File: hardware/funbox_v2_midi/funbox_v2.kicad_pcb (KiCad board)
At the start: 2 copper layers, 59.7 x 67.5 mm, 70 parts, among them J6 MIDI IN, J7 MIDI OUT, SW1 SW_SPDT, SW2 SW_SPDT, SW3 SW_SPDT, U1 TL074, U2 L7805, U5 H11L1

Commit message: Updated version2 pcb. Updated expression for Jupiter, Neptune, and Pluto
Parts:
- moved J7 1.85 mm to (175.8, 71.2)
- moved DipSwitch 1.82 mm to (124.1, 117.0)
- moved J6 1.62 mm to (119.9, 71.2)
- moved R31 0.96 mm to (154.4, 72.8)
- moved R33 0.96 mm to (162.1, 69.7)
- moved C6 0.45 mm to (131.1, 122.1)
- moved R32 0.28 mm to (141.4, 70.1)
- moved D2 0.27 mm to (133.8, 73.0)
- moved R30 0.27 mm to (133.8, 67.1)
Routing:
- net FOOT_SWITCH_2: track 77.6 -> 72.4 mm
- net DIP2: track 30.1 -> 25.5 mm
- net DIP1: track 23.9 -> 25.7 mm
- net MIDI_OUT_JACK_PIN5: track 27.4 -> 25.7 mm
- net MIDI_OUT: track 19.5 -> 21.1 mm
- net MIDI_IN_JACK_PIN5: track 17.7 -> 16.2 mm
- net DIP3: track 39.9 -> 38.6 mm
- net DIP4: track 41.0 -> 39.7 mm
- net MIDI_IN_JACK_PIN4: track 10.9 -> 9.74 mm
- net MIDI_IN: track 38.0 -> 36.9 mm
- net MIDI_OUT_JACK_PIN4: track 10.0 -> 9.15 mm
- net Net-(Out1-Pin_1): track 32.3 -> 31.7 mm
- net Net-(In2-Pin_1): track 45.5 -> 46.1 mm
- net GND: vias 0 -> 1

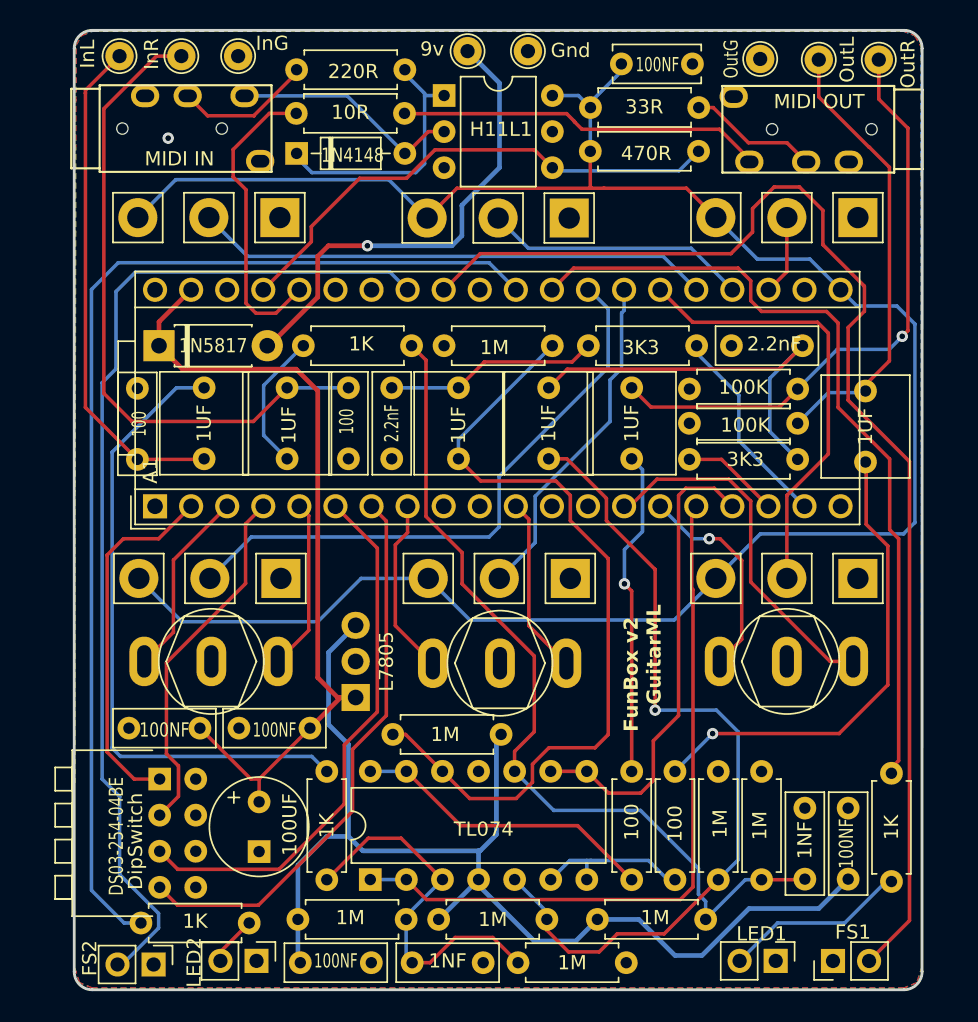
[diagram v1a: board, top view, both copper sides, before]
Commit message: Added pF label for clarity
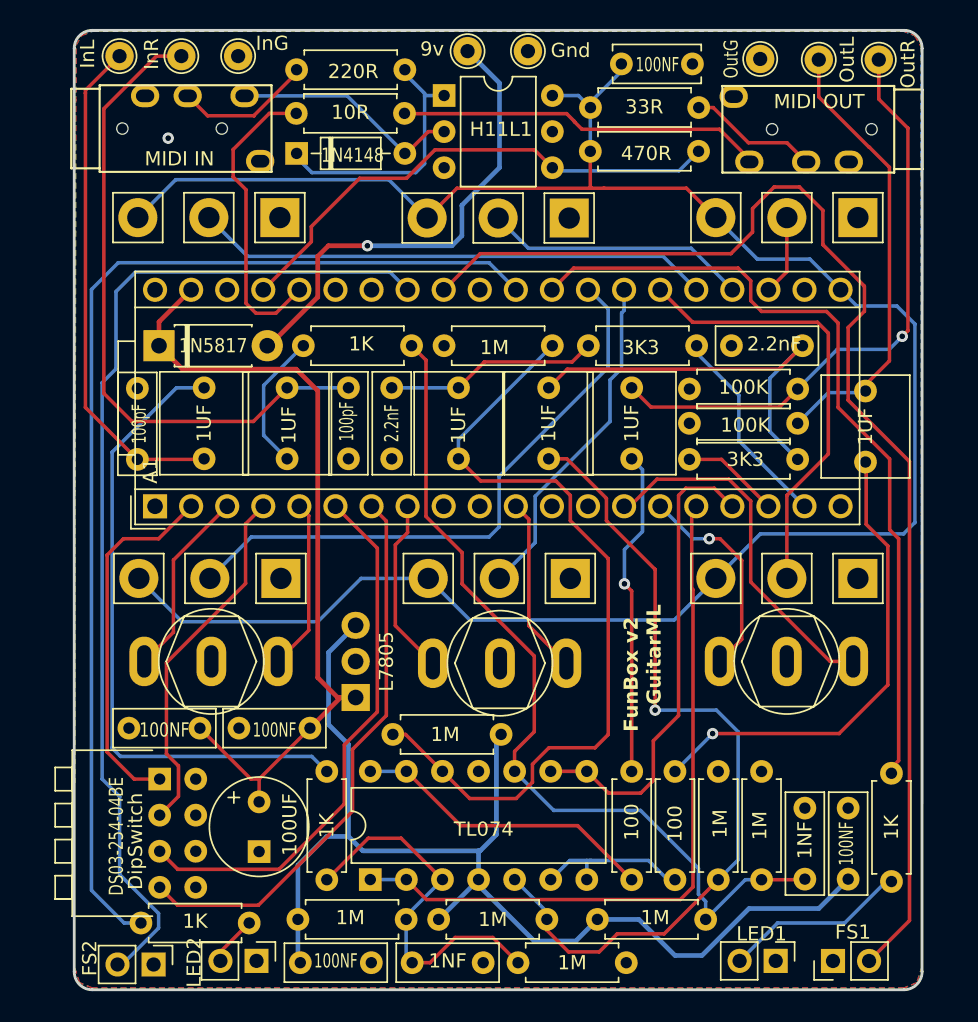
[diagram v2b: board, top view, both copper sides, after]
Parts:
- C11, C2: value 100 -> 100pF
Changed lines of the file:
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@@
         (effects (font (size 1 1) (thickness 0.15)))
     )
-    (fp_text value "100" (at 2.373 0.127 90) (layer "F.SilkS")
-        (effects (font (size 1 0.6952) (thickness 0.15)))
+    (fp_text value "100pF" (at 2.373 0.127 90) (layer "F.SilkS")
+        (effects (font (size 1 0.652) (thickness 0.15)))
     )
     (fp_text user "${REFERENCE}" (at 2.5 0 90) (layer "F.Fab")
@@
     )
     (fp_text value "100NF" (at 2.5 0.127 90) (layer "F.SilkS")
-        (effects (font (size 1 0.7968) (thickness 0.15)))
+        (effects (font (size 1 0.7) (thickness 0.15)))
     )
     (fp_text user "${REFERENCE}" (at 2.5 0 90) (layer "F.Fab")
@@
         (effects (font (size 1 1) (thickness 0.15)))
     )
-    (fp_text value "100" (at 2.5 0.127 90) (layer "F.SilkS")
-        (effects (font (size 1 0.6952) (thickness 0.15)))
+    (fp_text value "100pF" (at 2.5 0.127 90) (layer "F.SilkS")
+        (effects (font (size 1 0.652) (thickness 0.15)))
     )
     (fp_text user "${REFERENCE}" (at 2.5 0 90) (layer "F.Fab")
